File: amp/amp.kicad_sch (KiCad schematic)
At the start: 40 parts, among them J1 Input, J2 Speaker 8Ω, J3 Headphones, J6 FX Send, J7 FX Return, SW1 PWR, SW2 FX Enable/Bypass, U1 TL072

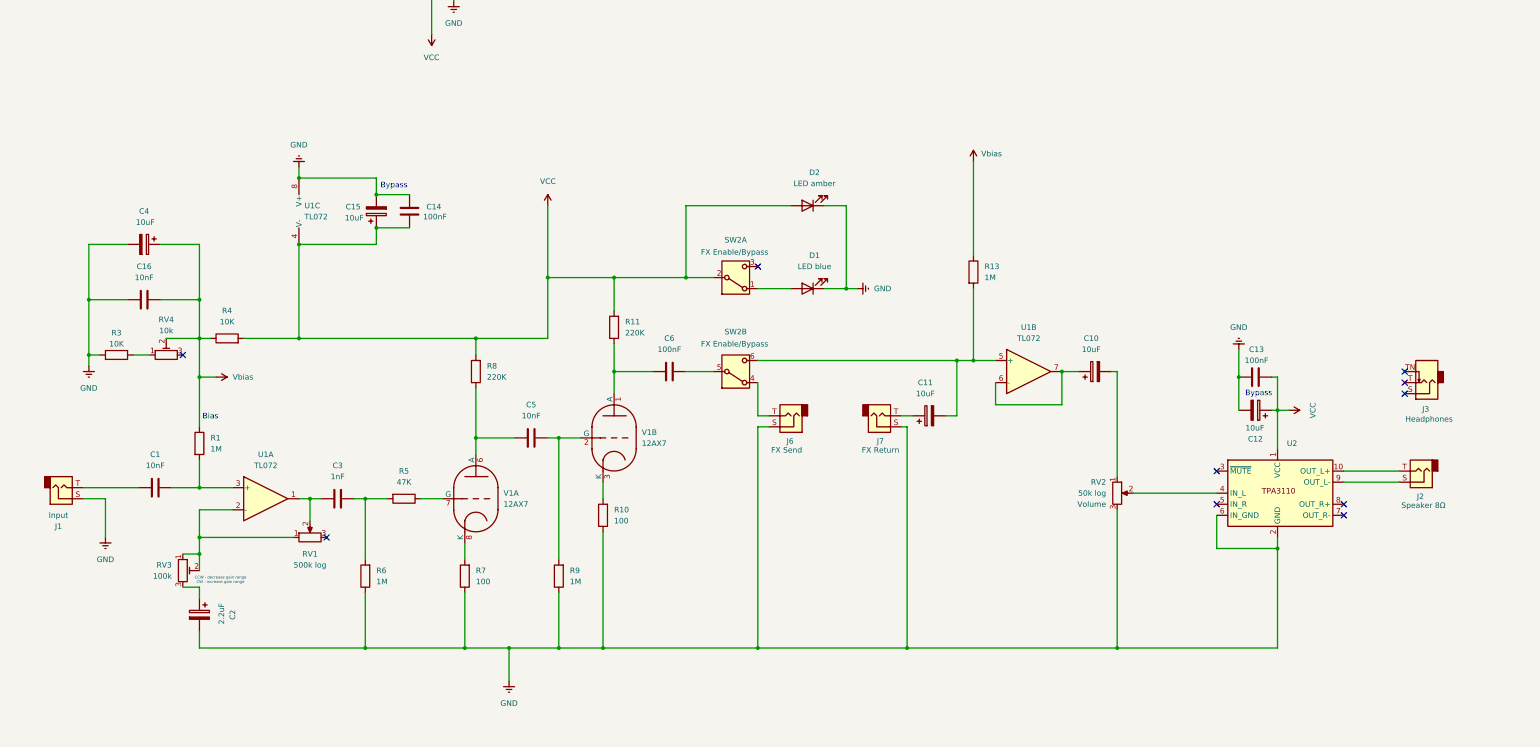
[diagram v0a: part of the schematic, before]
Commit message: Buffer triode outputs
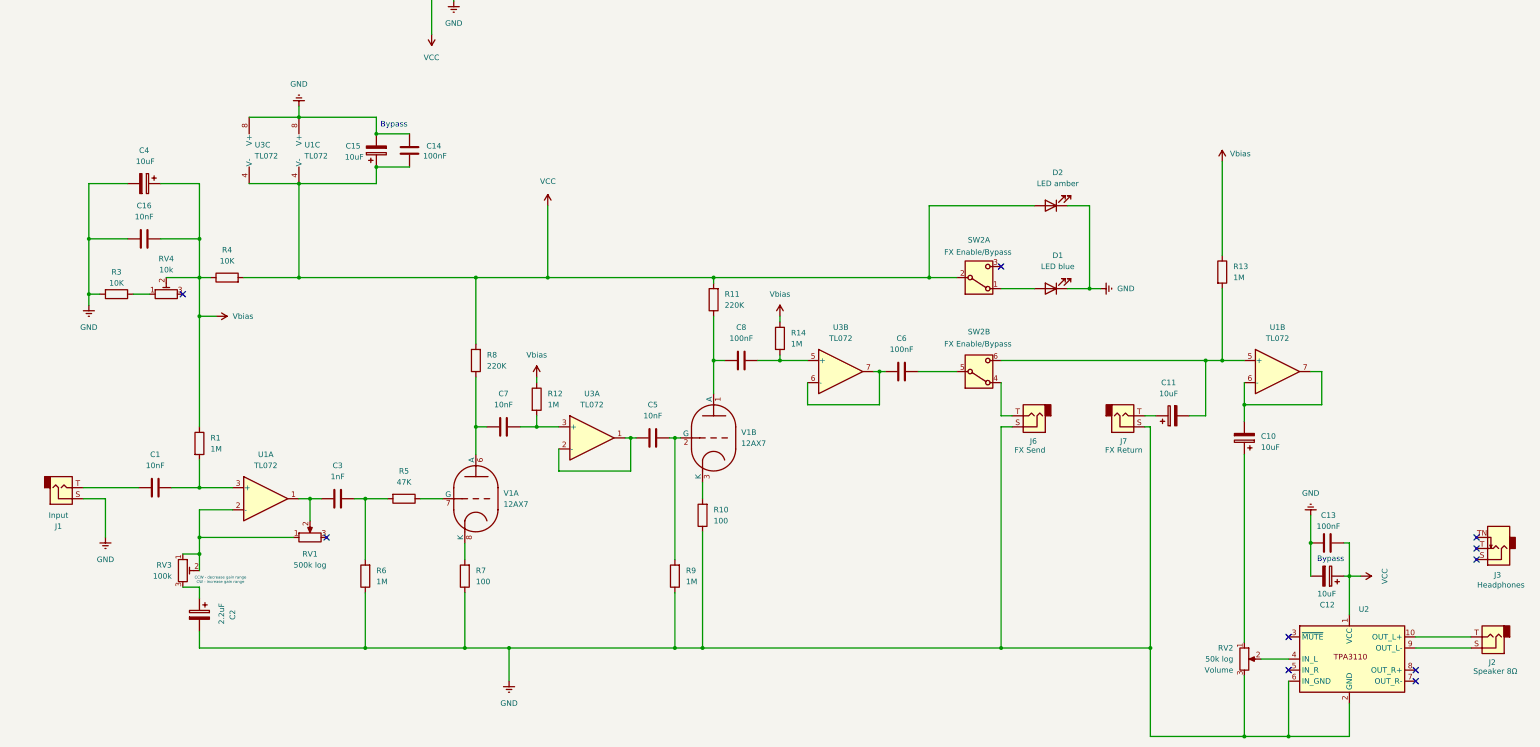
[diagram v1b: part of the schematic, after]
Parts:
- added C7: 10nF, symbol Device:C
- added C8: 100nF, symbol Device:C
- added R12, R14: 1M, symbol Device:R
- added U3: TL072, symbol Amplifier_Operational:TL072
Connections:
- net GND: now also U3.8 (V+)
- net VCC: now also U3.4 (V-)
- net Vbias: now also R12.1, R14.1
- net at U1.6 (-), U1.7: now also C10.2; no longer C10.1
- net at RV2.1: now also C10.1; no longer C10.2
- net at R11.1, V1.1 (A): now also C8.1; no longer C6.1
- net at R8.1, V1.6 (A): now also C7.1; no longer C5.1
- new net: C8.2, R14.2, U3.5 (+)
- new net: C6.1, U3.6 (-), U3.7
- new net: C7.2, R12.2, U3.3 (+)
- new net: C5.1, U3.1, U3.2 (-)
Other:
- note removed: "Bias"
- moved on the sheet: C10, C11, C12, C13, C14, C15, C16, C4, C5, C6, D1, D2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

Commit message: Tighten layout
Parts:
- renumbered U3 to U2, U2 to U3
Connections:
- net at C2.1: now also RV3.2; no longer RV3.3
- net at RV1.1, RV3.1, U1.2 (-): no longer RV3.2
- no-connect marks 11 -> 12
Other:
- note added: "Gain range CCW - decrease CW - increase"
- note removed: "CCW - decrease gain range CW - increase gain range"
- moved on the sheet: C10, C11, C12, C13, C14, C15, C2, C3, C5, C6, C7, C8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

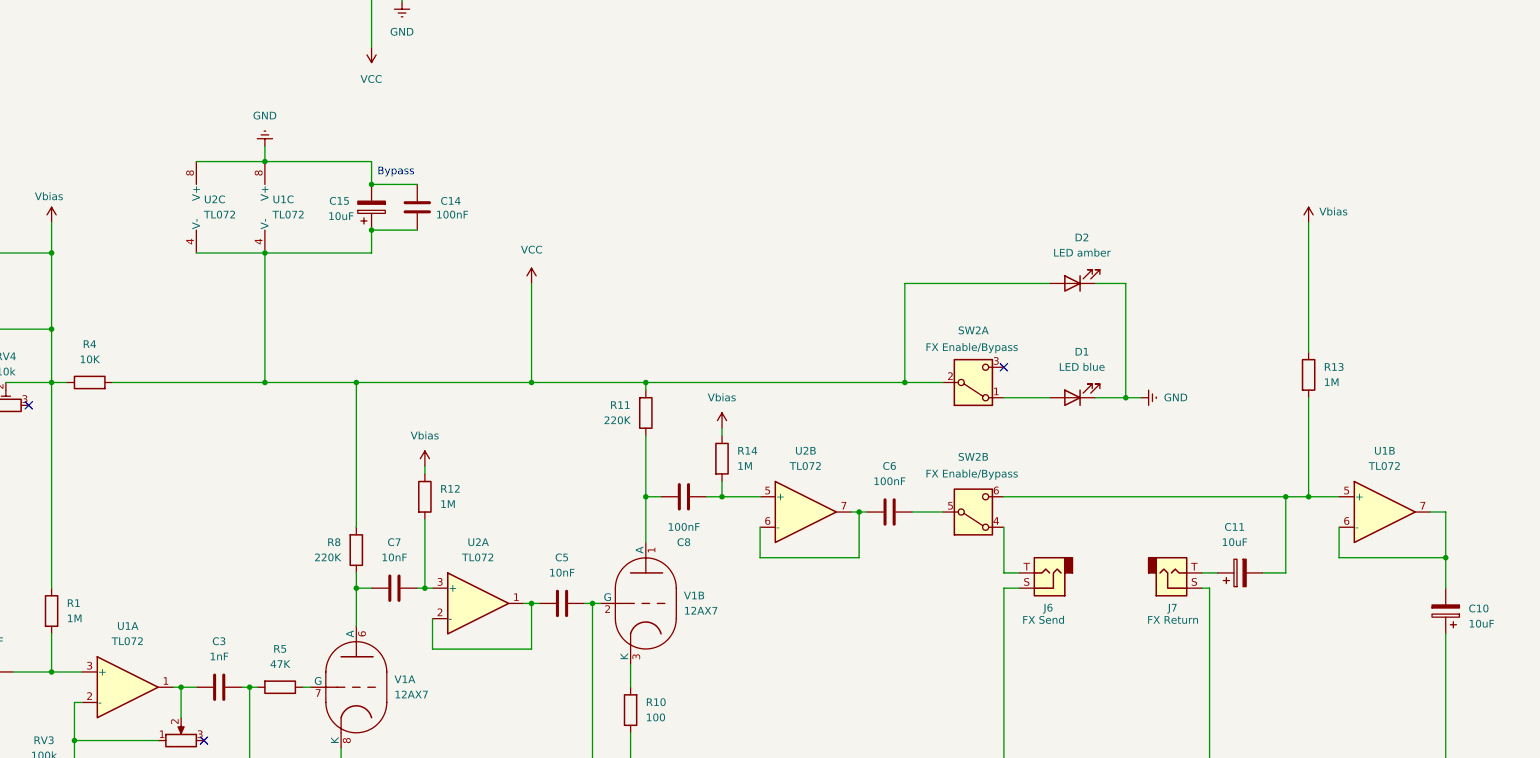
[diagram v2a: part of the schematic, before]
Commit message: Use TL074 instead of 2xTL072 for preamp
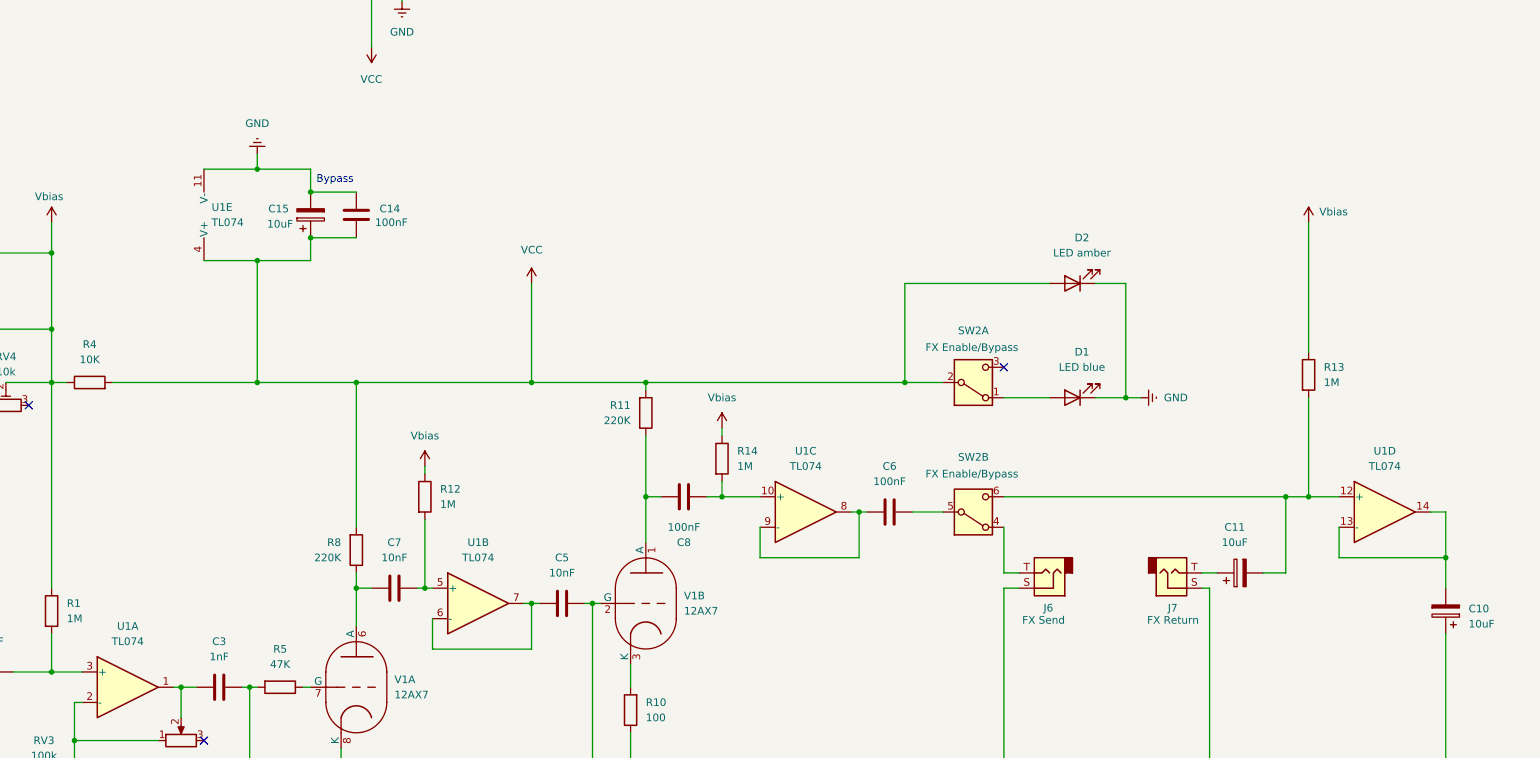
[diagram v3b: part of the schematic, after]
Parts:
- removed U1, U2: TL072, symbol Amplifier_Operational:TL072
- added U1: TL074, symbol Amplifier_Operational:TL074
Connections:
- net GND: now also U1.11 (V-)
- net VCC: now also U1.4 (V+)
- net at C10.2: now also U1.13 (-), U1.14
- net at C1.2, R1.2: now also U1.3 (+)
- net at C8.2, R14.2: now also U1.10 (+)
- net at C6.1: now also U1.8, U1.9 (-)
- net at C3.1, RV1.2: now also U1.1
- net at RV1.1, RV3.1: now also U1.2 (-)
- net at C7.2, R12.2: now also U1.5 (+)
- net at C5.1: now also U1.6 (-), U1.7
- net at C11.2, R13.2, SW2.6 (C): now also U1.12 (+)
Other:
- moved on the sheet: C14, C15

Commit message: Mute speaker PA when headphones are plugged in (#29)
Also includes some layout/readability improvements
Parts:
- removed J3: Headphones, symbol Connector_Audio:AudioJack2_SwitchT
- added J3: Headphones, symbol Connector_Audio:AudioJack3_Switch
- added Q1: S8050, symbol Transistor_BJT:Q_NPN_CBE
- added R15, R16: 10K, symbol Device:R
- added R17: 4K7, symbol Device:R
- J1: value Input -> HI Input
- RV1: value 500k log -> 500K log
- RV2: value 50k log -> 50K log
- RV3: value 100k -> 100K
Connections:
- net GND: now also J3.S, Q1.3 (E), R17.1
- net VCC: now also R15.2, R16.2
- net at U3.3 (~{MUTE}): now also Q1.1 (C), R16.1, R17.2
- new net: J3.SN, Q1.2 (B), R15.1
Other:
- note added: "CW increase CCW decrease"
- note added: "FX loop"
- note added: "Mute"
- note added: "Opamp bias"
- note added: "Opamp bypass"
- note added: "Power amp"
- note added: "Pre amp"
- note removed: "Gain range CCW - decrease CW - increase"
- company: (none) -> Maja Bojarska
- title: (none) -> Bumble Tuby Guitar Amplifier
- moved on the sheet: C1, C10, C11, C12, C13, C14, C15, C16, C2, C3, C4, C5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

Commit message: rename project sym lib to 'amp'
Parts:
- U3: symbol TPA3110_module:PCB_TPA3310 -> amp:PCB_TPA3310
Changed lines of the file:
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@@
 	)
 	(symbol
-		(lib_id "TPA3110_module:PCB_TPA3310")
+		(lib_id "amp:PCB_TPA3310")
 		(at 341.63 173.99 0)
 		(unit 1)
@@
 		(dnp no)
 		(property "Reference" "U3"
-			(at 340.868 160.528 0)
+			(at 346.964 160.782 0)
 			(effects
 				(font
 					(size 1.27 1.27)
 				)
-				(justify left)
 			)
 		)
 		(property "Value" "~"
-			(at 343.7733 161.29 0)
+			(at 341.63 173.99 0)
 			(effects
 				(font
 					(size 1.27 1.27)
 				)
-				(justify left)
 			)
 		)

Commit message: Impl polarity prot
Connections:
- net VCC: now also R16.1; no longer R16.2, SW1.2 (B)
- net at Q1.1 (C), R17.2, U3.3 (~{MUTE}): now also R16.2; no longer R16.1
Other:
- note added: "Power"
- note added: "TTL high pullup"
- moved on the sheet: C1, C10, C11, C12, C13, C14, C15, C2, C3, C5, C6, C7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

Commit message: split sections, label I/O netlists
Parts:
- removed C10: 10uF, symbol Device:C_Polarized
- added C17: 10uF, symbol Device:C_Polarized
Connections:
- net at RV2.1: now also C6.1
- net at U1.13 (-), U1.14: now also C17.1
- net at U1.8, U1.9 (-): now also C6.2; no longer C6.1
- net PRE_OUT: now reaches SW2.5 (B)
- net PRE_OUT: now also RV2.2; no longer C6.2
- net FX_OUT: now reaches U3.4 (IN_L)
- net FX_OUT: now also C17.2; no longer RV2.2
- net PRE_IN: now reaches C1.1, J1.T
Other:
- moved on the sheet: C1, C11, C12, C13, C14, C15, C16, C2, C3, C4, C5, C6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

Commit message: Headphone PA, line-in support, active signal mixing,  (#35)
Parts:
- added C10, C20: 220uF, symbol Device:C_Polarized
- added C18, C21: 47nF, symbol Device:C
- added C19, C9: 100uF, symbol Device:C_Polarized
- added C25: 10uF, symbol Device:C_Polarized
- added C26: 10nF, symbol Device:C
- added C27, C28, C29, C30, C31, C32: 1uF, symbol Device:C_Polarized
- added J4: LO Input, symbol Connector_Audio:AudioJack3
- added R18, R19: 10, symbol Device:R
- added R20, R24, R26, R27, R28, R29, R30, R31, R32, R33, R34: 10K, symbol Device:R
- added R23: 1M, symbol Device:R
- added RV5: 10k, symbol Device:R_Potentiometer_Trim
- added U2, U4: LM386, symbol Amplifier_Audio:LM386
- added U5, U6: NE5532, symbol Amplifier_Operational:NE5532
- C11, C17: value 10uF -> 1uF
- R13: value 1M -> 10K
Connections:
- net FX_OUT: now also RV2.3; no longer U3.4 (IN_L)
- net GND: now also R13.2, RV2.1, C18.1, C19.2, C21.1, C25.2, C26.1, C27.2, C9.2, J4.S, R20.1, U2.2 (-), U2.4 (GND), U4.2 (-), U4.4 (GND), U5.4 (V-), U6.4 (V-); no longer RV2.3
- net PRE_OUT: now also C6.1; no longer RV2.2
- net VCC: now also C27.1, R24.2, U2.6 (V+), U4.6 (V+), U5.8 (V+), U6.8 (V+)
- net ~{MUTE}: now reaches Q1.1 (C), R16.2, R17.2, U3.3 (~{MUTE})
- net at U3.5 (IN_R): now also R20.2
- net at C11.2, SW2.6 (C), U1.12 (+): now also R23.1; no longer R13.2
- net PHONE_R: now reaches J3.R
- net PHONE_R: now also C20.2
- net PHONE_L: now reaches J3.T
- net PHONE_L: now also C10.2
- net Vbias renamed Vb_pre
- net Vb_pre: now also R23.2; no longer R13.1
- new net: R32.2, R33.1, R34.1, U6.2 (-)
- new net: C19.1, U4.7 (BYPASS)
- new net: C9.1, U2.7 (BYPASS)
- new net: U6.6 (-), U6.7
- new net: C20.1, R19.1, U4.5
- new net: C10.1, R18.1, U2.5
- new net: C30.1, R31.1, U5.7
- new net: R29.1, R30.1, R31.2, U5.6 (-)
- new net: C21.2, R19.2
- new net: R13.1, RV5.1
- new net: R28.2, R29.2, RV2.2
- new net: C29.2, R27.2
- new net: C31.1, R26.1, U5.1
- new net: R26.2, R27.1, R28.1, U5.2 (-)
- new net: C32.1, R32.1, U6.1
- new net: C18.2, R18.2
- new net: C28.2, R30.2
- new net LINE_IN_L: C29.1, J4.T
- new net LINE_IN_R: C28.1, J4.R
- new net MIX_L: C31.2, R33.2, U2.3 (+)
- new net MIX_MONO: C32.2, U3.4 (IN_L)
- new net MIX_R: C30.2, R34.2, U4.3 (+)
- new net Vb_mix: C25.1, C26.2, R24.1, RV5.2, U5.3 (+), U5.5 (+), U6.3 (+), U6.5 (+)
- no-connect marks 12 -> 14
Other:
- note added: "Headphones"
- note added: "Mixer"
- note added: "Speaker"
- note added: "Zobel"
- note removed: "Bypass"
- moved on the sheet: C1, C11, C12, C13, C14, C15, C16, C17, C3, C4, C5, C6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
